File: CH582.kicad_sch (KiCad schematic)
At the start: 52 parts, among them J1 Conn_01x02, J2 Conn_01x02, J3 Peripherals, J4 USB, SW2 POWER, U2 XC6220B331QR-G, U3 M3406, U4 TP4056, Y1 32MHz, Y2 Crystal_Small

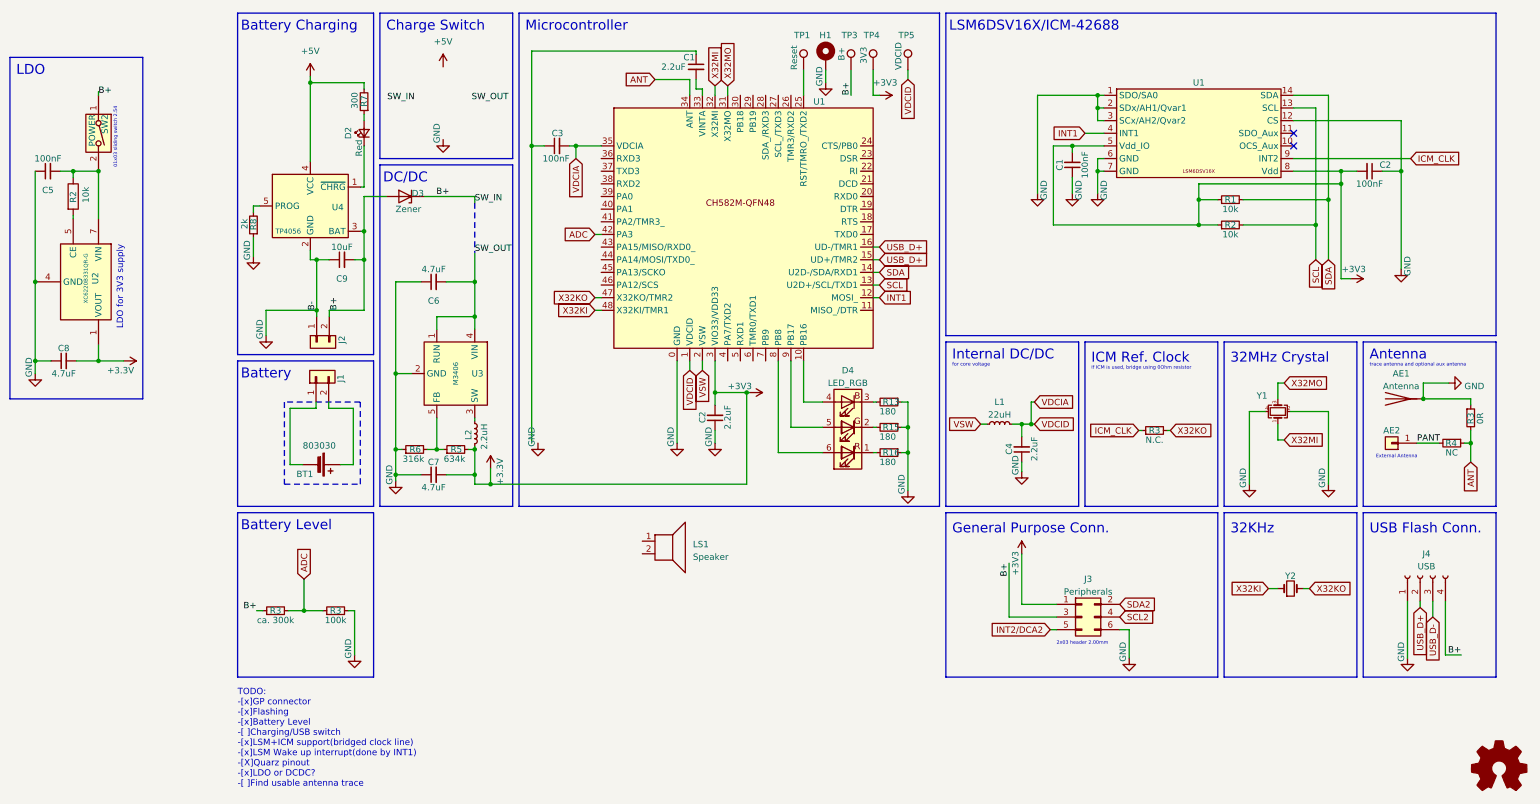
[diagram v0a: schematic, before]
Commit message: V1, aux not connected
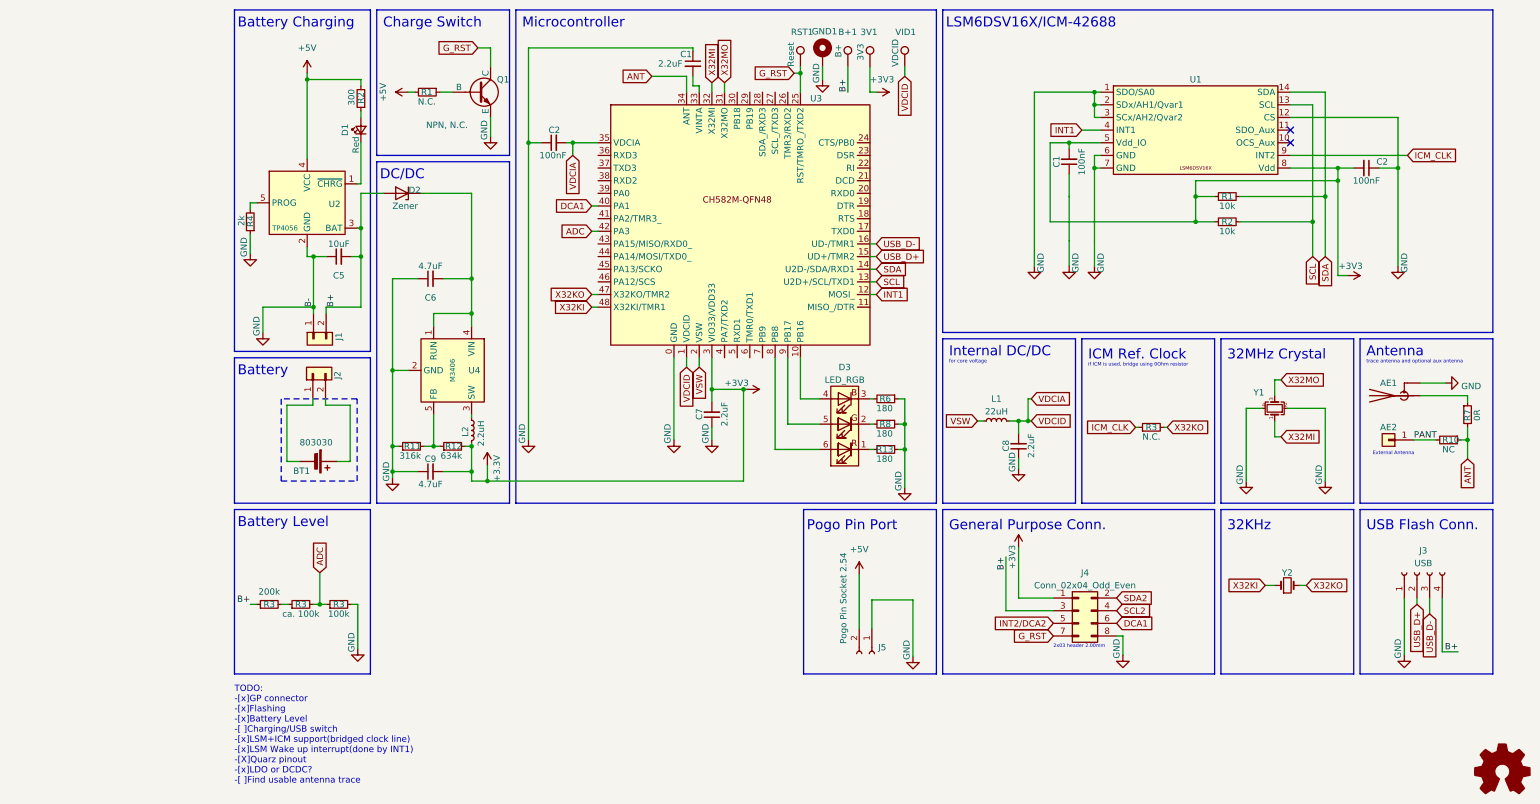
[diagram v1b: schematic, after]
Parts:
- removed AE1: Antenna, symbol Device:Antenna
- removed C5: 100nF, Capacitor_SMD:C_1206_3216Metric_Pad1.33x1.80mm_HandSolder, symbol Device:C_Small
- removed C8: 4.7uF, Capacitor_SMD:C_1206_3216Metric_Pad1.33x1.80mm_HandSolder, symbol Device:C_Small
- removed J3: Peripherals, symbol Connector_Generic:Conn_02x03_Odd_Even
- removed LS1: Speaker, symbol Device:Speaker
- removed R2: 10k, Resistor_SMD:R_0805_2012Metric_Pad1.20x1.40mm_HandSolder, symbol Device:R
- removed SW2: POWER, Connector_PinSocket_2.54mm:PinSocket_1x03_P2.54mm_Vertical, symbol Switch:SW_DIP_x01
- removed U2: XC6220B331QR-G, Package_SO:HTSOP-8-1EP_3.9x4.9mm_P1.27mm_EP2.4x3.2mm, symbol Custom:XC6220B331QR-G
- added AE1: Antenna_Shield, RF_Antenna:Texas_SWRA117D_2.4GHz_Right, symbol Device:Antenna_Shield
- added J4: Conn_02x04_Odd_Even, Connector_FFC-FPC:Hirose_FH12-8S-0.5SH_1x08-1MP_P0.50mm_Horizontal, symbol Connector_Generic:Conn_02x04_Odd_Even
- added J5: Pogo Pin Socket 2.54, Connector_PinSocket_2.54mm:PinSocket_1x02_P2.54mm_Horizontal, symbol Connector:Conn_01x02_Socket
- added Q1: NPN, N.C., Package_TO_SOT_SMD:SOT-23, symbol Simulation_SPICE:NPN
- added R1: N.C., Resistor_SMD:R_0402_1005Metric, symbol Device:R_Small
- added R3: 200k, Resistor_SMD:R_0402_1005Metric, symbol Device:R_Small
- 3V1: renamed from TP4; footprint (none) -> Inductor_SMD:L_Changjiang_FNR5020S
- AE2: footprint (none) -> RF_Antenna:Johanson_2450AT18x100
- B+1: renamed from TP3; footprint (none) -> TestPoint:TestPoint_Pad_D1.0mm
- C1: footprint (none) -> Capacitor_SMD:C_0603_1608Metric
- C1, C2: footprint Capacitor_SMD:C_0805_2012Metric_Pad1.18x1.45mm_HandSolder -> Capacitor_SMD:C_0402_1005Metric
- C2: renamed from C3; footprint (none) -> Capacitor_SMD:C_0402_1005Metric
- C5: renamed from C9; footprint Capacitor_SMD:C_1206_3216Metric_Pad1.33x1.80mm_HandSolder -> Capacitor_SMD:C_0603_1608Metric
- C6: footprint Capacitor_SMD:C_1206_3216Metric_Pad1.33x1.80mm_HandSolder -> Capacitor_SMD:C_0603_1608Metric
- C7: renamed from C2; footprint (none) -> Capacitor_SMD:C_0603_1608Metric
- C8: renamed from C4; footprint (none) -> Capacitor_SMD:C_0603_1608Metric
- C9: renamed from C7; footprint Capacitor_SMD:C_1206_3216Metric_Pad1.33x1.80mm_HandSolder -> Capacitor_SMD:C_0603_1608Metric
- D1: renamed from D2; footprint (none) -> LED_SMD:LED_0603_1608Metric
- D2: renamed from D3; footprint (none) -> Diode_SMD:D_0603_1608Metric
- D3: renamed from D4; footprint (none) -> LED_SMD:LED_RGB_5050-6
- GND1: renamed from H1; footprint (none) -> MountingHole:MountingHole_2.2mm_M2_ISO14580_Pad_TopBottom
- J1: renamed from J2; footprint (none) -> Connector_PinHeader_2.00mm:PinHeader_1x02_P2.00mm_Vertical
- J3: renamed from J4; footprint (none) -> Connector_PinHeader_2.54mm:PinHeader_1x04_P2.54mm_Vertical
- L1: footprint (none) -> Inductor_SMD:L_Changjiang_FNR4020S
- L2: footprint (none) -> Inductor_SMD:L_Changjiang_FNR252010S
- R1, R2, R3: footprint Resistor_SMD:R_0805_2012Metric_Pad1.20x1.40mm_HandSolder -> Resistor_SMD:R_0402_1005Metric
- R10: renamed from R4; footprint (none) -> Resistor_SMD:R_0402_1005Metric
- R11: renamed from R6; footprint (none) -> Resistor_SMD:R_0402_1005Metric
- R12: renamed from R5; footprint (none) -> Resistor_SMD:R_0402_1005Metric
- R13: renamed from R16; footprint (none) -> Resistor_SMD:R_0402_1005Metric
- R2: renamed from R7; footprint (none) -> Resistor_SMD:R_0402_1005Metric
- R3: value ca. 300k -> ca. 100k; footprint Resistor_SMD:R_0805_2012Metric_Pad1.20x1.40mm_HandSolder -> Resistor_SMD:R_0402_1005Metric
- R4: renamed from R8; footprint (none) -> Resistor_SMD:R_0402_1005Metric
- R6: renamed from R13; footprint (none) -> Resistor_SMD:R_0402_1005Metric
- R7: renamed from R3; footprint (none) -> Resistor_SMD:R_0402_1005Metric
- R8: renamed from R15; footprint (none) -> Resistor_SMD:R_0402_1005Metric
- RST1: renamed from TP1; footprint (none) -> TestPoint:TestPoint_Pad_D1.0mm
- U2: renamed from U4; footprint (none) -> Package_TO_SOT_SMD:SOT-23-5
- U3: renamed from U1; footprint (none) -> Package_DFN_QFN:QFN-48-1EP_5x5mm_P0.35mm_EP3.7x3.7mm_ThermalVias
- U4: renamed from U3; footprint (none) -> Package_TO_SOT_SMD:SOT-23-5
- VID1: renamed from TP5; footprint (none) -> TestPoint:TestPoint_Pad_D1.0mm
- Y1: footprint (none) -> Crystal:Crystal_SMD_2016-4Pin_2.0x1.6mm
- Y2: footprint (none) -> Crystal:Crystal_SMD_2012-2Pin_2.0x1.2mm
- renumbered J1 to J2
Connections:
- net +3V3: now also J4.1 (Pin_1)
- net +5V: now also J5.2 (Pin_2), R1.2
- net B+: now also J4.3 (Pin_3), R3.1; no longer D2.1 (K), R3.1
- net GND: now also C1.1, C2.1, AE1.2 (Shield), J4.8 (Pin_8), J5.1 (Pin_1), Q1.3 (E); no longer R7.1
- net INT2/DCA2: now also J4.5 (Pin_5)
- net SCL2: now also J4.4 (Pin_4)
- net SDA2: now also J4.2 (Pin_2)
- net USB_D+: no longer U3.16 (UD-/TMR1)
- net USB_D-: now also U3.16 (UD-/TMR1)
- net G_RST: now reaches RST1.1, U3.25 (RST/TMRO_/TXD2)
- net G_RST: now also J4.7 (Pin_7), Q1.1 (C)
- net DCA1: now reaches U3.40 (PA1)
- net DCA1: now also J4.6 (Pin_6)
- net SW_OUT: no longer names the net of C6.2, U4.1 (RUN), U4.4 (VIN)
- net SW_OUT: now also D2.1 (K)
- new net: Q1.2 (B), R1.1
- new net: AE1.1 (A), R7.1
- new net: R3.1, R3.2
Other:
- note added: "Pogo Pin Port"
- note removed: "01x03 sliding switch 2.54"
- note removed: "LDO"
- note removed: "LDO for 3V3 supply"
- moved on the sheet: 3V1, AE2, B+1, BT1, C1, C2, C5, C6, C7, C8, C9, D1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

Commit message: goodbye 0.1mm
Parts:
- 3V1: footprint Inductor_SMD:L_Changjiang_FNR5020S -> TestPoint:TestPoint_Pad_D1.0mm
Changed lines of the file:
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@@
       (effects (font (size 1.27 1.27)) (justify left))
     )
-    (property "Footprint" "Inductor_SMD:L_Changjiang_FNR5020S" (at 153.67 33.02 0)
+    (property "Footprint" "TestPoint:TestPoint_Pad_D1.0mm" (at 153.67 33.02 0)
       (effects (font (size 1.27 1.27)) hide)
     )

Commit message: final tweaks 1
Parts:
- added R1: 200k, Resistor_SMD:R_0402_1005Metric, symbol Device:R_Small
- D2: value Zener -> Schottky
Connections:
- net GND: now also R1.1
- net ICM_CLK: now also R1.2
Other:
- note added: "FCC Aux."
- note removed: "General Purpose Conn."
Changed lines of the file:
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@@
   (junction (at 155.575 104.775) (diameter 0) (color 0 0 0 0)
   )
+  (junction (at 259.588 50.8) (diameter 0) (color 0 0 0 0)
+  )
   (junction (at 134.62 34.29) (diameter 0) (color 0 0 0 0)
   )
@@
     (stroke (width 0) (type default))
   )
+  (wire (pts (xy 259.588 44.958) (xy 259.588 50.8))
+    (stroke (width 0) (type default))
+  )
   (wire (pts (xy 44.196 112.268) (xy 44.196 100.965))
     (stroke (width 0) (type default))
@@
     (stroke (width 0) (type default))
   )
+  (wire (pts (xy 259.588 50.8) (xy 259.588 55.372))
+    (stroke (width 0) (type default))
+  )
   (wire (pts (xy 233.045 50.8) (xy 256.54 50.8))
     (stroke (width 0) (type dash))
@@
     (stroke (width 0) (type default))
   )
+  (wire (pts (xy 259.588 50.8) (xy 256.54 50.8))
+    (stroke (width 0) (type default))
+  )
   (wire (pts (xy 72.39 43.18) (xy 72.39 46.99))
     (stroke (width 0) (type default))
@@
     (stroke (width 0) (type default))
   )
+  (wire (pts (xy 259.588 60.452) (xy 259.588 73.152))
+    (stroke (width 0) (type default))
+  )
   (wire (pts (xy 227.965 137.16) (xy 229.87 137.16))
     (stroke (width 0) (type default))
@@
     (effects (font (size 2 2)) (justify left bottom))
   )
-  (text "General Purpose Conn." (at 164.465 126.365 0)
+  (text "FCC Aux." (at 164.465 126.365 0)
     (effects (font (size 2 2)) (justify left bottom))
   )
@@
     )
   )
-  (global_label "ICM_CLK" (shape input) (at 256.54 50.8 0) (fields_autoplaced)
+  (global_label "ICM_CLK" (shape input) (at 259.588 44.958 90) (fields_autoplaced)
     (effects (font (size 1.27 1.27)) (justify left))
-    (property "Intersheetrefs" "${INTERSHEET_REFS}" (at 267.3077 50.8 0)
+    (property "Intersheetrefs" "${INTERSHEET_REFS}" (at 259.588 34.1903 90)
       (effects (font (size 1.27 1.27)) (justify left) hide)
     )
@@
     )
   )
+  (symbol (lib_id "Device:R_Small") (at 259.588 57.912 180) (unit 1)
+    (in_bom yes) (on_board yes) (dnp no)
+    (property "Reference" "R1" (at 259.588 57.912 90)
+      (effects (font (size 1.27 1.27)))
+    )
+    (property "Value" "200k" (at 261.493 57.912 90)
+      (effects (font (size 1.27 1.27)))
+    )
+    (property "Footprint" "Resistor_SMD:R_0402_1005Metric" (at 259.588 57.912 0)
+      (effects (font (size 1.27 1.27)) hide)
+    )
+    (property "Datasheet" "~" (at 259.588 57.912 0)
+      (effects (font (size 1.27 1.27)) hide)
+    )
+    (pin "1")
+    (pin "2")
+    (instances
+      (project "LSM6D breakout"
+        (path "/588f6831-0b32-432d-8fad-feddef935df9"
+          (reference "R1") (unit 1)
+        )
+      )
+      (project "CH582"
+        (path "/5e1a16ae-7d88-49c0-aee0-e35b69a10f89"
+          (reference "R17") (unit 1)
+        )
+      )
+    )
+  )
   (symbol (lib_id "Custom:CH582M") (at 121.92 64.77 0) (unit 1)
     (in_bom yes) (on_board yes) (dnp no) (fields_autoplaced)
@@
     )
   )
+  (symbol (lib_id "power:GND") (at 259.588 73.152 0) (unit 1)
+    (in_bom yes) (on_board yes) (dnp no)
+    (property "Reference" "#PWR04" (at 259.588 79.502 0)
+      (effects (font (size 1.27 1.27)) hide)
+    )
+    (property "Value" "GND" (at 260.858 72.517 90)
+      (effects (font (size 1.27 1.27)))
+    )
+    (property "Footprint" "" (at 259.588 73.152 0)
+      (effects (font (size 1.27 1.27)) hide)
+    )
+    (property "Datasheet" "" (at 259.588 73.152 0)
+      (effects (font (size 1.27 1.27)) hide)
+    )
+    (pin "1")
+    (instances
+      (project "LSM6D breakout"
+        (path "/588f6831-0b32-432d-8fad-feddef935df9"
+          (reference "#PWR04") (unit 1)
+        )
+      )
+      (project "CH582"
+        (path "/5e1a16ae-7d88-49c0-aee0-e35b69a10f89"
+          (reference "#PWR030") (unit 1)
+        )
+      )
+    )
+  )
   (symbol (lib_id "Device:D_Zener") (at 54.61 58.42 180) (unit 1)
     (in_bom yes) (on_board yes) (dnp no)
@@
       (effects (font (size 1.27 1.27)))
     )
-    (property "Value" "Zener" (at 55.245 60.96 0)
+    (property "Value" "Schottky" (at 55.245 60.96 0)
       (effects (font (size 1.27 1.27)))
     )

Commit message: V1, order version
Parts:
- added C1: 10nF, Capacitor_SMD:C_0402_1005Metric, symbol Device:C_Small
- added TCK1: SWD_TCK, TestPoint:TestPoint_Pad_D1.0mm, symbol Connector:TestPoint
- R1: value 200k -> N.C.
- renumbered R10 to R11, R11 to R12, R12 to R13, R13 to R14, R4 to R5, R6 to R7, R7 to R8, R8 to R9
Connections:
- net ADC: now also C1.1
- net GND: now also C1.2
- net TCK: now reaches U3.11 (MISO_/DTR)
- net TCK: now also TCK1.1

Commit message: V02
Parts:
- removed D2: Schottky, Diode_SMD:D_0603_1608Metric, symbol Device:D_Zener
- removed GND1: MountingHole_Pad, MountingHole:MountingHole_2.2mm_M2_ISO14580_Pad_TopBottom, symbol Mechanical:MountingHole_Pad
- removed Q1: NPN, N.C., Package_TO_SOT_SMD:SOT-23, symbol Simulation_SPICE:NPN
- added GND1: GND, TestPoint:TestPoint_Pad_D1.0mm, symbol Connector:TestPoint
- added R18: 0, Resistor_SMD:R_0603_1608Metric, symbol Device:R_Small
- added R19: 20k, Resistor_SMD:R_0603_1608Metric, symbol Device:R_Small
- C1, C2: footprint Capacitor_SMD:C_0402_1005Metric -> Capacitor_SMD:C_0603_1608Metric
- J5: footprint Connector_PinSocket_2.54mm:PinSocket_1x02_P2.54mm_Horizontal -> Library:PinSocket_1x02_P2.54mm_Horizontal
- R1: value N.C. -> 10k; footprint Resistor_SMD:R_0402_1005Metric -> Resistor_SMD:R_0603_1608Metric
- R1, R11, R14, R2, R3, R5, R7, R8, R9: footprint Resistor_SMD:R_0402_1005Metric -> Resistor_SMD:R_0603_1608Metric
- R12: value 316k -> 180k; footprint Resistor_SMD:R_0402_1005Metric -> Resistor_SMD:R_0603_1608Metric
- R13: value 634k -> 810k; footprint Resistor_SMD:R_0402_1005Metric -> Resistor_SMD:R_0603_1608Metric
- U2: value TP4056 -> PJ4054B
- U3: footprint Package_DFN_QFN:QFN-48-1EP_5x5mm_P0.35mm_EP3.7x3.7mm_ThermalVias -> Library:QFN 48 fixed
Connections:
- net SCL2 is gone; now on net SCL: J4.4 (Pin_4)
- net SDA2 is gone; now on net SDA: J4.2 (Pin_2)
- net B+: now also R18.2; no longer C5.2, J3.4 (Pin_4), J4.3 (Pin_3)
- net GND: now also GND1.1, R19.2
- net G_RST: now also R1.1, U3.46 (PA12/SCS), R19.1; no longer U3.25 (RST/TMRO_/TXD2)
- net INT2/DCA2: now also U3.41 (PA2/TMR3_)
- net DBG+: now reaches C6.2, U4.1 (RUN), U4.4 (VIN)
- net DBG+: now also C5.2, J3.4 (Pin_4), J4.3 (Pin_3), R18.1
- net at D3.4 (BA): now also U3.8 (PB8); no longer U3.10 (PB16)
- net at D3.6 (RA): now also U3.10 (PB16); no longer U3.8 (PB8)
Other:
- note added: "Reset Switch"
- note removed: "Charge Switch"
- moved on the sheet: C5, R5
